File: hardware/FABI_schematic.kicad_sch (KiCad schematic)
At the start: 40 parts, among them J11 009159005551906, J11_GND1 Conn_01x01_Male, J11_VDD1 Conn_01x01_Male, J11_data1 Conn_01x01_Male, J12 Conn_01x04_Socket, J2 display_connector_91601-304LF, Q1 BSS806, U1 D5V0F4U6SO, U2 SC0918 (PicoW), U3 TSOP4838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

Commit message: v3.5: - swapped +/- connection of battery (as they are delivered normally) - fixing of footprints: FC68125 throws an error with a NPTH, fixed - fixed Pico W footprint, was not really possible to solder the SMD header with the shorted pads - updated SCH PDF & iBOM
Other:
- company: AsTeRICS Foundation -> AsTeRICS Foundation / Assistronik
- title: FABI3 PCB (PicoW) with 5 jack plugs -> FABI3 PCB (Pico2W) with 5 jack plugs
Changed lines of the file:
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@@
 	(paper "A4")
 	(title_block
-		(title "FABI3 PCB (PicoW) with 5 jack plugs")
-		(date "2023-08-23")
-		(rev "v3.1")
-		(company "AsTeRICS Foundation")
-		(comment 1 "www.asterics-foundation.org")
-		(comment 2 "Benjamin Aigner")
+		(title "FABI3 PCB (Pico2W) with 5 jack plugs")
+		(date "2025-08-12")
+		(rev "v3.5")
+		(company "AsTeRICS Foundation / Assistronik")
+		(comment 1 "https://www.asterics-foundation.org")
+		(comment 2 "https://assistronik.info")
+		(comment 3 "Benjamin Aigner")
 	)
 	(text "PN532\nNFC"

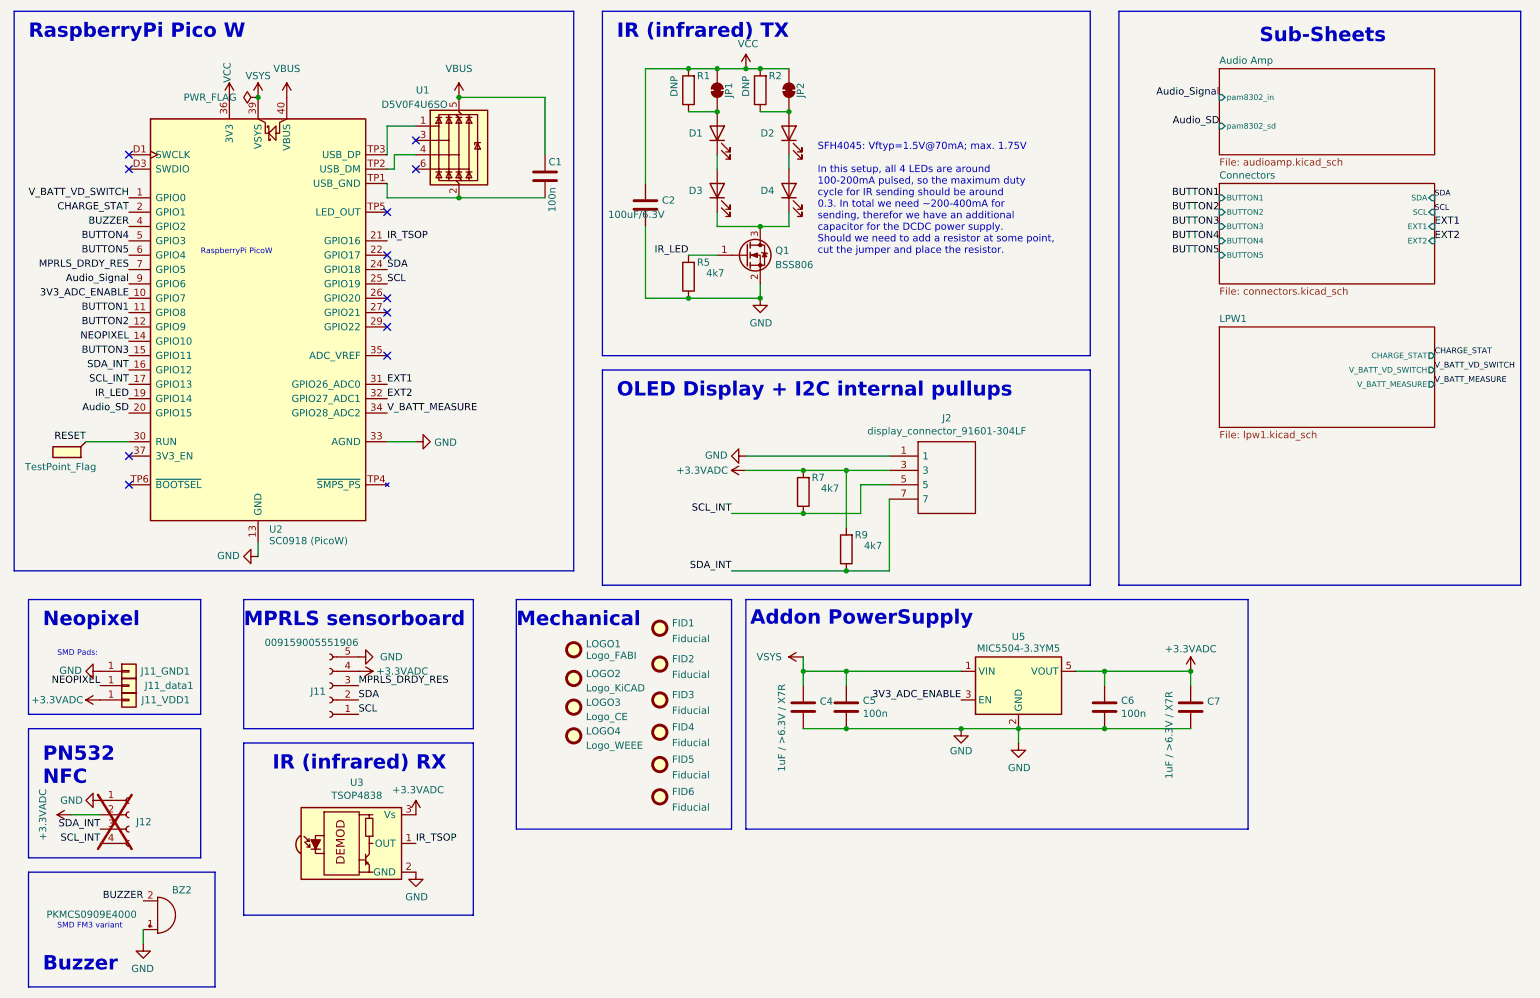
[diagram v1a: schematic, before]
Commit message: Added WS2812B footprint on front; for SMT assembly instead of soldering a Neopixel strip
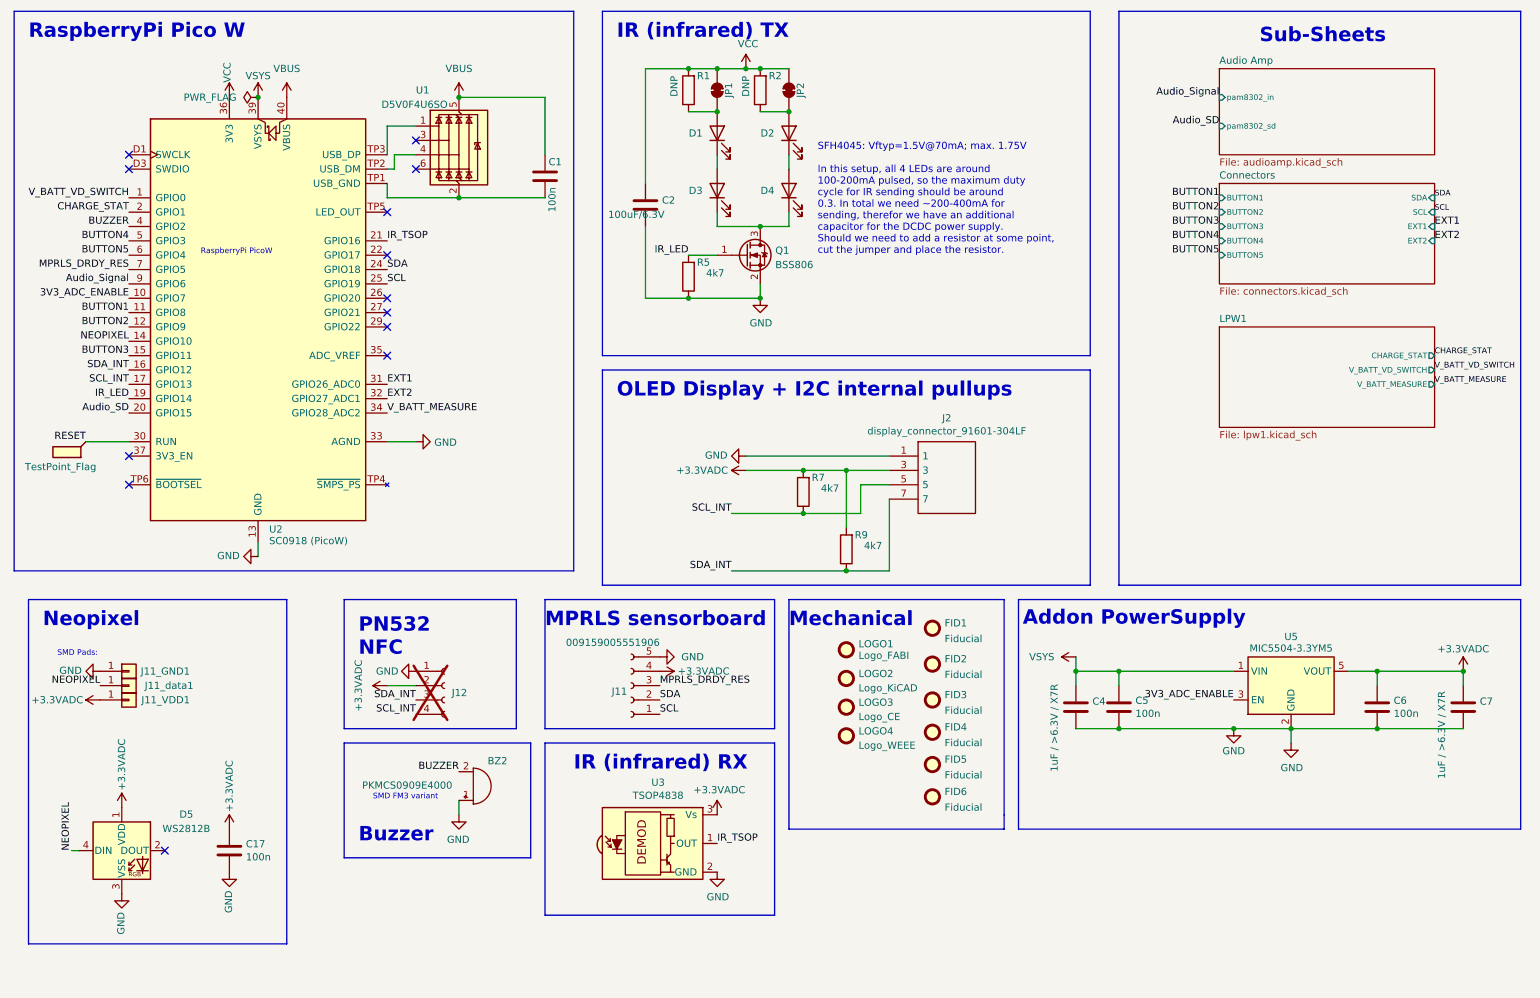
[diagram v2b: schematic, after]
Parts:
- added C17: 100n, Capacitor_SMD:C_0603_1608Metric, symbol Device:C
- added D5: WS2812B, LED_SMD:LED_WS2812B_PLCC4_5.0x5.0mm_P3.2mm, symbol LED:WS2812B
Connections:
- net +3.3VADC: now also C17.1, D5.1 (VDD)
- net GND: now also C17.2, D5.3 (VSS)
- net NEOPIXEL: now also D5.4 (DIN)
- no-connect marks 12 -> 13
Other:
- moved on the sheet: BZ2, C4, C5, C6, C7, FID1, FID2, FID3, FID4, FID5, FID6, J11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
